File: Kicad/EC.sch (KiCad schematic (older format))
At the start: 18 parts, among them U1 MCP6244

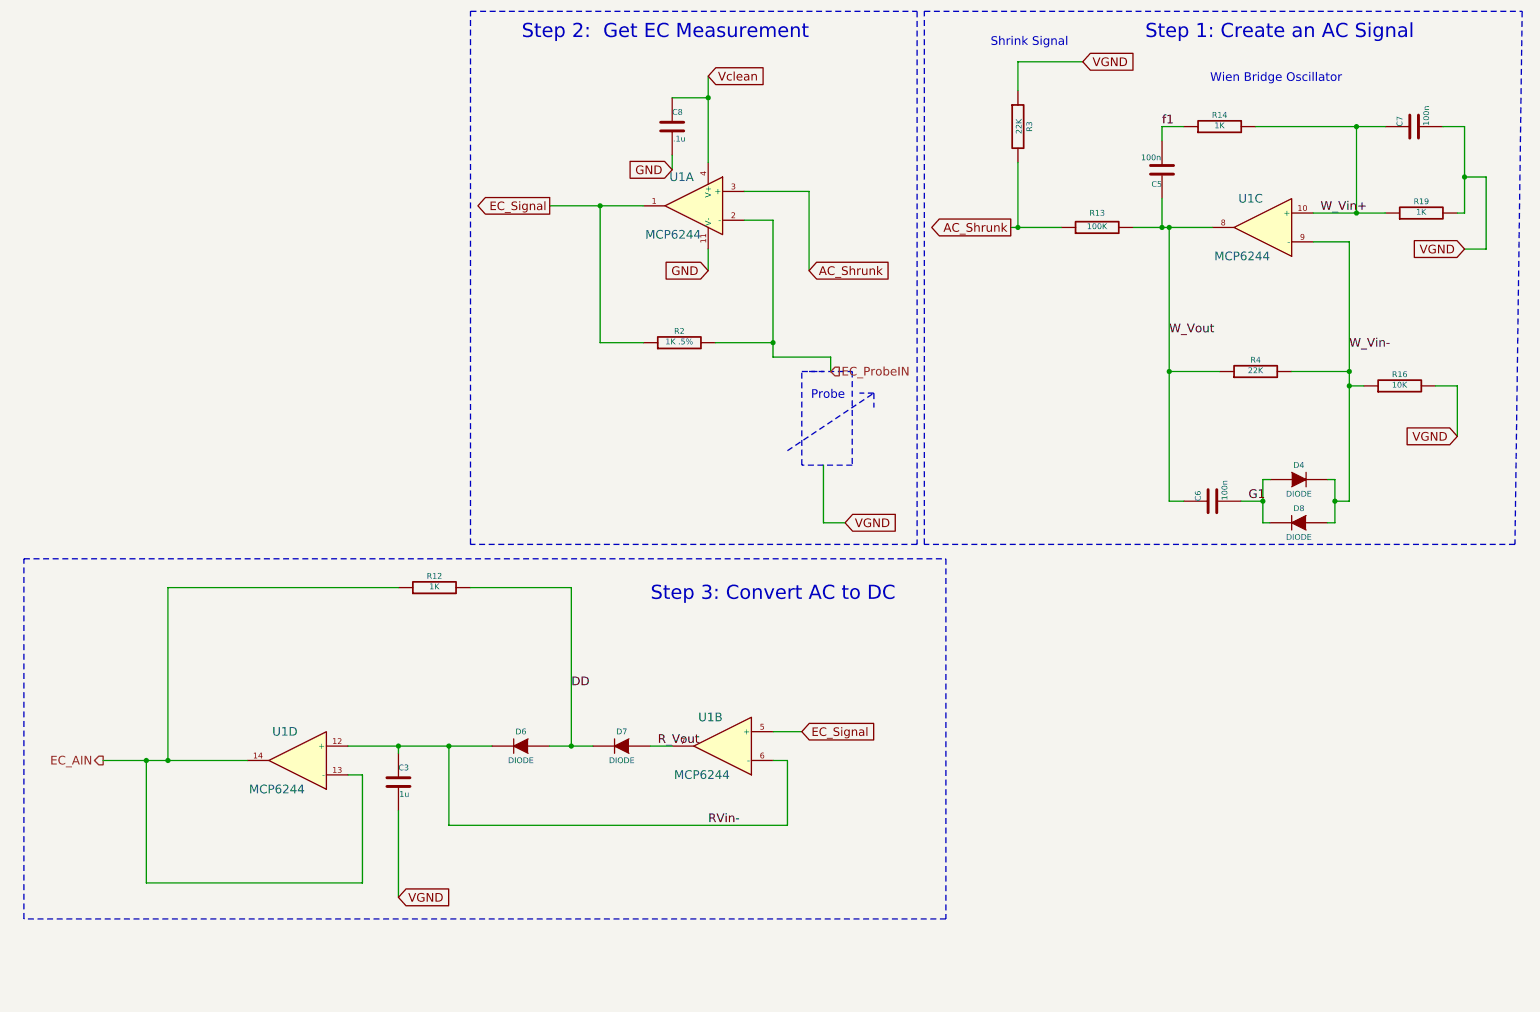
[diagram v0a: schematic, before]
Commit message: added ECTest Arduino Sketch also updates (not all) to the Schematic
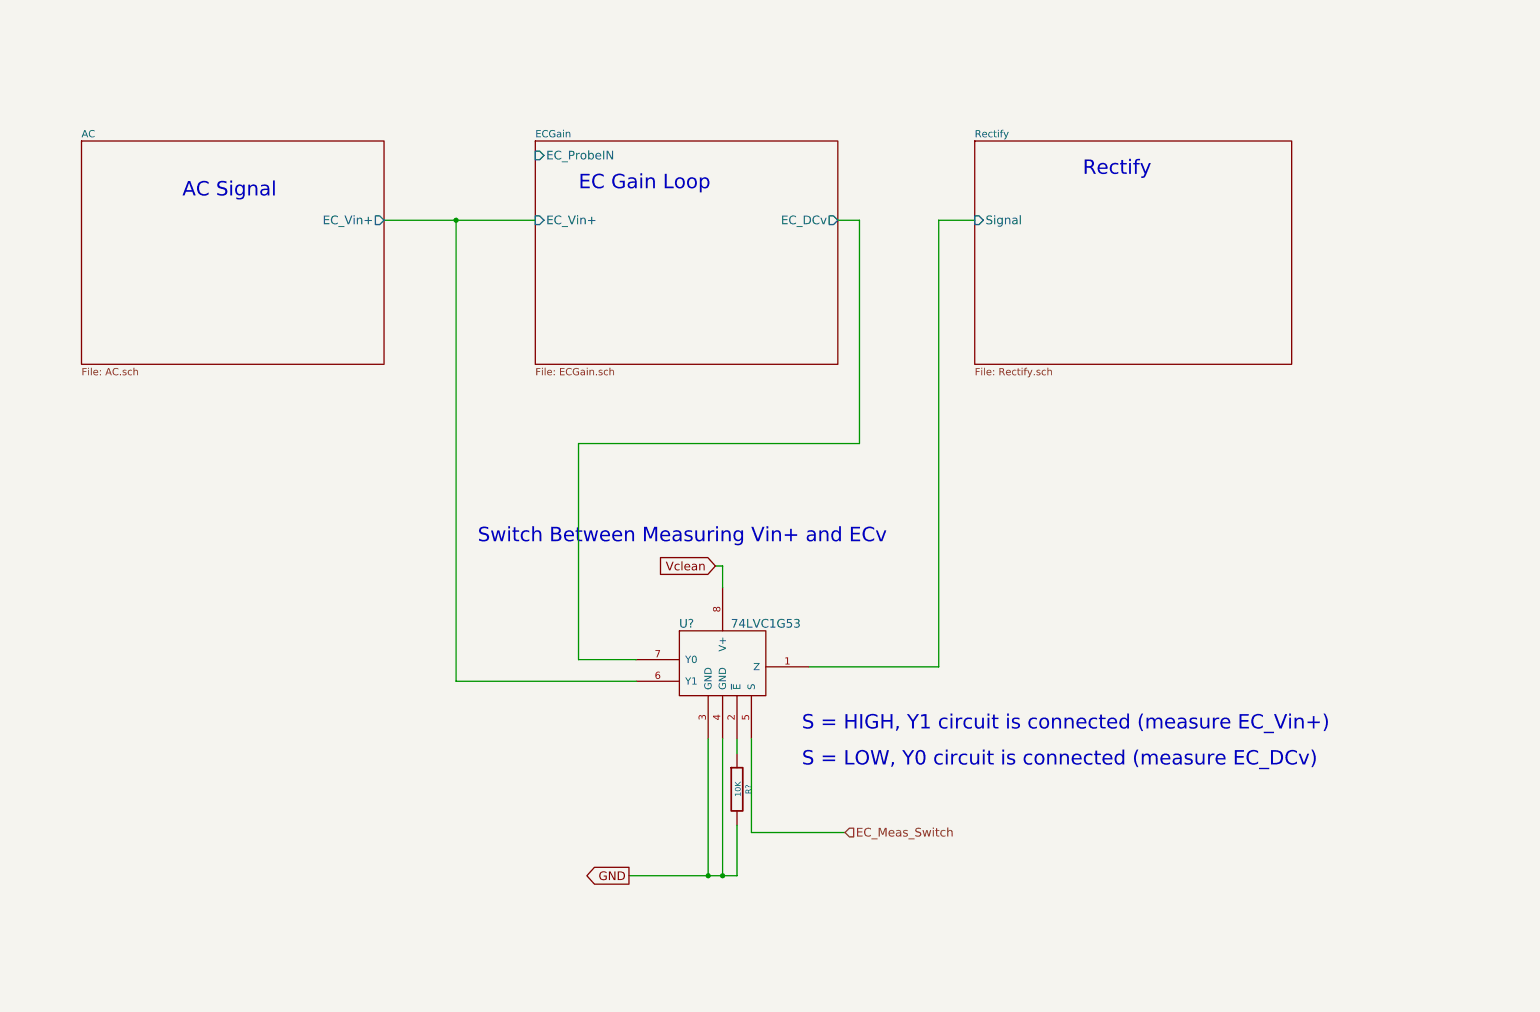
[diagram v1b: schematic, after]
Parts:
- removed C3: 1u, ~, symbol C
- removed C5, C6, C7: 100n, ~, symbol C
- removed C8: .1u, ~, symbol C
- removed D4, D6, D7, D8: DIODE, ~, symbol DIODE
- removed R12, R14, R19: 1K, ~, symbol R
- removed R13: 100K, ~, symbol R
- removed R16: 10K, ~, symbol R
- removed R2: 1K .5%, ~, symbol R
- removed R3, R4: 22K, ~, symbol R
- removed U1: MCP6244, ~, symbol MCP6244
- added R?: 10K, ~, symbol R
- added U?: 74LVC1G53, ~, symbol 74LVC1G53
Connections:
- net GND: now also R?.2, U?.3 (GND), U?.4 (GND)
- net Vclean: now also U?.8 (V+)
- new net: R?.1, U?.2 (~E)
- new net AC/EC_Vin+: U?.6 (Y1)
- new net ECGain/EC_DCv: U?.7 (Y0)
- new net EC_Meas_Switch: U?.5 (S)
- new net Rectify/Signal: U?.1 (Z)
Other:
- note added: "AC Signal"
- note added: "EC Gain Loop\n"
- note added: "Rectify\n"
- note added: "S = HIGH, Y1 circuit is connected (measure EC_Vin+)"
- note added: "S = LOW, Y0 circuit is connected (measure EC_DCv)"
- note added: "Switch Between Measuring Vin+ and ECv\n"
- note removed: "Probe"
- note removed: "Shrink Signal"
- note removed: "Step 1: Create an AC Signal"
- note removed: "Step 2: Get EC Measurement"
- note removed: "Step 3: Convert AC to DC"
- note removed: "Wien Bridge Oscillator"

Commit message: layout for Alpha 2
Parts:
- gave numbers to parts that had none: 2
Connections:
- net AC/EC_Vin+: now also U1.7 (Y0); no longer U1.6 (Y1)
- net ECGain/EC_DCv: now also U1.6 (Y1); no longer U1.7 (Y0)
- net MUX_enable_pin: now reaches R2.1, U1.2 (~E)
- net EC_Meas_Switch renamed MUX_out_pin
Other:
- note added: "S = HIGH, Y1 circuit is connected (measure EC_DCv)"
- note added: "S = LOW, Y0 circuit is connected (measure EC_Vin+)"
- note removed: "S = HIGH, Y1 circuit is connected (measure EC_Vin+)"
- note removed: "S = LOW, Y0 circuit is connected (measure EC_DCv)"
- moved on the sheet: R2
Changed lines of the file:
@@
 Sheet 5 11
 Title ""
-Date "29 jan 2015"
+Date "8 feb 2015"
 Rev ""
 Comp ""
@@
 D9 E2 BF C4 18 F7 0C 4B 5E B4 8D 6F 67 A1 70 71 C5 12 A3 BD DD C9 B3 93 77 93 9B 2B F6 BC 6A 4C
 31 A6 9D A4 5C 5A 6D B5 D5 56 5B 6D B5 D5 02 ED 0F 8F D8 15 DB 22 89 0B B4 00 00 00 00 49 45 4E
-44 AE 42 60 82 A9 $EndBitmap
+44 AE 42 60 82 67 $EndBitmap
 EndData
 $EndBitmap
@@
 EC Gain Loop\n
 $Bitmap
-Pos 5350 2650
+Pos 5350 2750
 Scale 1.000000
 Data
@@
 12 D7 1E 39 D3 97 8B E9 CC 09 7E A4 21 84 7B DE 75 BE 6C 10 1D B1 C0 C8 E6 44 20 98 58 88 D3 4B
 BF A4 FE AC E7 27 87 F5 F3 E7 B2 6E 04 7A D3 5E FF 1F 0B 1A 44 E2 12 6D EC E1 00 00 00 00 49 45
-4E 44 AE 42 60 82 68 $EndBitmap
+4E 44 AE 42 60 82 6A $EndBitmap
 EndData
 $EndBitmap
@@
 Rectify\n
 $Comp
-L 74LVC1G53 U?
+L 74LVC1G53 U1
 U 1 1 54C7A3D8
 P 5350 5200
-F 0 "U?" H 5400 5350 60  0000 C CNN
+F 0 "U1" H 5400 5350 60  0000 C CNN
 F 1 "74LVC1G53" H 5950 5350 60  0000 C CNN
 F 2 "~" H 5450 4800 60  0000 C CNN
@@
 	1    0    0    -1
 $EndComp
-Text Notes 3950 4500 0    100  ~ 0
+Text Notes 6300 5550 0    100  ~ 0
 Switch Between Measuring Vin+ and ECv\n
 Wire Wire Line
 	3300 2250 4350 2250
-Wire Wire Line
-	3800 2250 3800 5450
-Wire Wire Line
-	3800 5450 5050 5450
-Connection ~ 3800 2250
-Wire Wire Line
-	6450 2250 6600 2250
-Wire Wire Line
-	6600 2250 6600 3800
-Wire Wire Line
-	6600 3800 4650 3800
-Wire Wire Line
-	4650 3800 4650 5300
-Wire Wire Line
-	4650 5300 5050 5300
 $Sheet
 S 7400 1700 2200 1550
@@
 F1 "Rectify.sch" 50
 F2 "Signal" I L 7400 2250 60
+F3 "EC_AIN" O R 9600 2400 60
+F4 "FET_pin" I R 9600 2700 60
 $EndSheet
 Wire Wire Line
@@
 Wire Wire Line
 	7150 2250 7400 2250
-Text GLabel 5000 6800 0    60   Output ~ 0
+Text GLabel 4900 7600 0    60   Output ~ 0
 GND
 Wire Wire Line
-	5000 6800 5750 6800
-Wire Wire Line
-	5650 5850 5650 6800
+	5650 5850 5650 7600
 $Comp
-L R R?
+L R R2
 U 1 1 54C7AE26
-P 5750 6200
-F 0 "R?" V 5830 6200 40  0000 C CNN
-F 1 "10K" V 5757 6201 40  0000 C CNN
-F 2 "~" V 5680 6200 30  0000 C CNN
-F 3 "~" H 5750 6200 30  0000 C CNN
-	1    5750 6200
+P 5750 7200
+F 0 "R2" V 5830 7200 40  0000 C CNN
+F 1 "10K" V 5757 7201 40  0000 C CNN
+F 2 "~" V 5680 7200 30  0000 C CNN
+F 3 "~" H 5750 7200 30  0000 C CNN
+	1    5750 7200
 	1    0    0    -1
 $EndComp
 Wire Wire Line
-	5550 6800 5550 5850
-Connection ~ 5550 6800
-Wire Wire Line
-	5750 5950 5750 5850
-Wire Wire Line
-	5750 6800 5750 6450
-Connection ~ 5650 6800
+	5550 5850 5550 7600
 Text HLabel 6500 6500 2    60   Input ~ 0
-EC_Meas_Switch
+MUX_out_pin
 Wire Wire Line
 	5850 5850 5850 6500
@@
 	5650 4650 5600 4650
 Text Notes 6200 5800 0    100  ~ 0
-S = HIGH, Y1 circuit is connected (measure EC_Vin+)
+S = LOW, Y0 circuit is connected (measure EC_Vin+)
 Text Notes 6200 6050 0    100  ~ 0
-S = LOW, Y0 circuit is connected (measure EC_DCv)
+S = HIGH, Y1 circuit is connected (measure EC_DCv)
+Text HLabel 10750 2700 2    60   Input ~ 0
+FET_pin
+Wire Wire Line
+	9600 2700 10750 2700
+Text HLabel 10750 2400 2    60   Output ~ 0
+EC_AIN
+Wire Wire Line
+	9600 2400 10750 2400
+Wire Wire Line
+	3750 2250 3750 5300
+Wire Wire Line
+	3750 5300 5050 5300
+Connection ~ 3750 2250
+Wire Wire Line
+	6450 2250 6700 2250
+Wire Wire Line
+	6700 2250 6700 4200
+Wire Wire Line
+	6700 4200 4750 4200
+Wire Wire Line
+	4750 4200 4750 5450
+Wire Wire Line
+	4750 5450 5050 5450
+Wire Wire Line
+	5750 5850 5750 6950
+Wire Wire Line
+	5750 6650 6500 6650
+Text HLabel 6500 6650 2    60   Input ~ 0
+MUX_enable_pin
+Connection ~ 5750 6650
+Wire Wire Line
+	4900 7600 5750 7600
+Wire Wire Line
+	5750 7600 5750 7450
+Connection ~ 5650 7600
+Connection ~ 5550 7600
+Text HLabel 1400 1100 0    60   Input ~ 0
+EC_ProbeIN
+Wire Wire Line
+	1400 1100 4100 1100
+Wire Wire Line
+	4100 1100 4100 1800
+Wire Wire Line
+	4100 1800 4350 1800
 $EndSCHEMATC

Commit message: updated layout prior to sending to OshPark
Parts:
- added C8: .1u, ~, symbol C
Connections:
- net GND: now also C8.2; no longer R2.2
- net Vclean: now also R2.2, C8.1
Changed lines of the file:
@@
 Sheet 5 11
 Title ""
-Date "8 feb 2015"
+Date "9 feb 2015"
 Rev ""
 Comp ""
@@
 D9 E2 BF C4 18 F7 0C 4B 5E B4 8D 6F 67 A1 70 71 C5 12 A3 BD DD C9 B3 93 77 93 9B 2B F6 BC 6A 4C
 31 A6 9D A4 5C 5A 6D B5 D5 56 5B 6D B5 D5 02 ED 0F 8F D8 15 DB 22 89 0B B4 00 00 00 00 49 45 4E
-44 AE 42 60 82 67 $EndBitmap
+44 AE 42 60 82 D3 $EndBitmap
 EndData
 $EndBitmap
@@
 12 D7 1E 39 D3 97 8B E9 CC 09 7E A4 21 84 7B DE 75 BE 6C 10 1D B1 C0 C8 E6 44 20 98 58 88 D3 4B
 BF A4 FE AC E7 27 87 F5 F3 E7 B2 6E 04 7A D3 5E FF 1F 0B 1A 44 E2 12 6D EC E1 00 00 00 00 49 45
-4E 44 AE 42 60 82 6A $EndBitmap
+4E 44 AE 42 60 82 79 $EndBitmap
 EndData
 $EndBitmap
@@
 GND
 Wire Wire Line
-	5650 5850 5650 7600
+	5650 7600 5650 5850
 $Comp
 L R R2
@@
 Wire Wire Line
 	5850 6500 6500 6500
-Text GLabel 5600 4650 0    60   Input ~ 0
+Text GLabel 5650 4350 0    60   Input ~ 0
 Vclean
 Wire Wire Line
-	5650 4800 5650 4650
-Wire Wire Line
-	5650 4650 5600 4650
+	5650 4350 5650 4800
 Text Notes 6200 5800 0    100  ~ 0
 S = LOW, Y0 circuit is connected (measure EC_Vin+)
@@
 MUX_enable_pin
 Connection ~ 5750 6650
-Wire Wire Line
-	4900 7600 5750 7600
-Wire Wire Line
-	5750 7600 5750 7450
-Connection ~ 5650 7600
-Connection ~ 5550 7600
 Text HLabel 1400 1100 0    60   Input ~ 0
 EC_ProbeIN
@@
 Wire Wire Line
 	4100 1800 4350 1800
+Wire Wire Line
+	4900 7600 5650 7600
+Connection ~ 5550 7600
+Wire Wire Line
+	5750 7450 5750 7500
+Wire Wire Line
+	5750 7500 6000 7500
+Text GLabel 6000 7500 2    60   Input ~ 0
+Vclean
+$Comp
+L C C8
+U 1 1 54D91F94
+P 6350 4800
+F 0 "C8" H 6350 4900 40  0000 L CNN
+F 1 ".1u" H 6356 4715 40  0000 L CNN
+F 2 "~" H 6388 4650 30  0000 C CNN
+F 3 "~" H 6350 4800 60  0000 C CNN
+	1    6350 4800
+	1    0    0    -1
+$EndComp
+Wire Wire Line
+	6350 4600 6350 4500
+Wire Wire Line
+	6350 4500 5650 4500
+Connection ~ 5650 4500
+Wire Wire Line
+	6350 5150 6350 5000
+Text GLabel 6350 5150 2    60   Input ~ 0
+GND
 $EndSCHEMATC

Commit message: Beta 2 sent to OSHPark
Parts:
- removed R2: 10K, ~, symbol R
- added TP1: Vin, symbol CONN_1
- added TP4: Vout, symbol CONN_1
- added VP1: S, symbol CONN_1
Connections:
- net MUX_enable_pin is gone; now on net GND: U1.2 (~E)
- net Rectify/Signal: now also VP1.1
- net AC/EC_Vin+ renamed AC/EC_Vin
- net AC/EC_Vin: now also TP1.1
- net ECGain/EC_DCv renamed ECGain/EC_Vout
- net ECGain/EC_Vout: now also TP4.1
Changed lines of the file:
@@
 $Descr A4 11693 8268
 encoding utf-8
-Sheet 5 11
+Sheet 5 10
 Title ""
-Date "9 feb 2015"
+Date "26 mar 2015"
 Rev ""
 Comp ""
@@
 F0 "AC" 50
 F1 "AC.sch" 50
-F2 "EC_Vin+" O R 3300 2250 60
+F2 "EC_Vin" O R 3300 2250 60
 $EndSheet
 Text Notes 1900 2100 0    100  ~ 0
@@
 D9 E2 BF C4 18 F7 0C 4B 5E B4 8D 6F 67 A1 70 71 C5 12 A3 BD DD C9 B3 93 77 93 9B 2B F6 BC 6A 4C
 31 A6 9D A4 5C 5A 6D B5 D5 56 5B 6D B5 D5 02 ED 0F 8F D8 15 DB 22 89 0B B4 00 00 00 00 49 45 4E
-44 AE 42 60 82 D3 $EndBitmap
+44 AE 42 60 82 FE $EndBitmap
 EndData
 $EndBitmap
@@
 F1 "ECGain.sch" 50
 F2 "EC_ProbeIN" I L 4350 1800 60
-F3 "EC_Vin+" I L 4350 2250 60
-F4 "EC_DCv" O R 6450 2250 60
+F3 "EC_Vin" I L 4350 2250 60
+F4 "EC_Vout" O R 6450 2250 60
 $EndSheet
 Text Notes 4650 2050 0    100  ~ 0
@@
 12 D7 1E 39 D3 97 8B E9 CC 09 7E A4 21 84 7B DE 75 BE 6C 10 1D B1 C0 C8 E6 44 20 98 58 88 D3 4B
 BF A4 FE AC E7 27 87 F5 F3 E7 B2 6E 04 7A D3 5E FF 1F 0B 1A 44 E2 12 6D EC E1 00 00 00 00 49 45
-4E 44 AE 42 60 82 79 $EndBitmap
+4E 44 AE 42 60 82 75 $EndBitmap
 EndData
 $EndBitmap
@@
 Wire Wire Line
 	5650 7600 5650 5850
-$Comp
-L R R2
-U 1 1 54C7AE26
-P 5750 7200
-F 0 "R2" V 5830 7200 40  0000 C CNN
-F 1 "10K" V 5757 7201 40  0000 C CNN
-F 2 "~" V 5680 7200 30  0000 C CNN
-F 3 "~" H 5750 7200 30  0000 C CNN
-	1    5750 7200
-	1    0    0    -1
-$EndComp
 Wire Wire Line
 	5550 5850 5550 7600
@@
 	4750 5450 5050 5450
 Wire Wire Line
-	5750 5850 5750 6950
-Wire Wire Line
-	5750 6650 6500 6650
-Text HLabel 6500 6650 2    60   Input ~ 0
-MUX_enable_pin
-Connection ~ 5750 6650
+	5750 7600 5750 5850
 Text HLabel 1400 1100 0    60   Input ~ 0
 EC_ProbeIN
@@
 	4100 1800 4350 1800
 Wire Wire Line
-	4900 7600 5650 7600
+	4900 7600 5750 7600
 Connection ~ 5550 7600
-Wire Wire Line
-	5750 7450 5750 7500
-Wire Wire Line
-	5750 7500 6000 7500
-Text GLabel 6000 7500 2    60   Input ~ 0
-Vclean
 $Comp
 L C C8
@@
 Text GLabel 6350 5150 2    60   Input ~ 0
 GND
+Connection ~ 5650 7600
+$Comp
+L CONN_1 TP1
+U 1 1 5513DDA8
+P 4050 3850
+F 0 "TP1" H 4130 3850 40  0001 L CNN
+F 1 "Vin" H 4050 3905 30  0000 C CNN
+F 2 "" H 4050 3850 60  0000 C CNN
+F 3 "" H 4050 3850 60  0000 C CNN
+	1    4050 3850
+	1    0    0    -1
+$EndComp
+Wire Wire Line
+	3900 3850 3750 3850
+Connection ~ 3750 3850
+$Comp
+L CONN_1 TP4
+U 1 1 5513DE76
+P 6300 3600
+F 0 "TP4" H 6380 3600 40  0001 L CNN
+F 1 "Vout" H 6300 3655 30  0000 C CNN
+F 2 "" H 6300 3600 60  0000 C CNN
+F 3 "" H 6300 3600 60  0000 C CNN
+	1    6300 3600
+	-1   0    0    1
+$EndComp
+Wire Wire Line
+	6450 3600 6700 3600
+Connection ~ 6700 3600
+$Comp
+L CONN_1 VP1
+U 1 1 5513DEEA
+P 7500 3900
+F 0 "VP1" H 7580 3900 40  0001 L CNN
+F 1 "S" H 7500 3955 30  0000 C CNN
+F 2 "" H 7500 3900 60  0000 C CNN
+F 3 "" H 7500 3900 60  0000 C CNN
+	1    7500 3900
+	1    0    0    -1
+$EndComp
+Wire Wire Line
+	7350 3900 7150 3900
+Connection ~ 7150 3900
 $EndSCHEMATC
